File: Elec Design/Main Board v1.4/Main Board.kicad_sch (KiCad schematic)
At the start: 64 parts, among them J1 PJ-102A, J3 Conn_ARM_JTAG_SWD_10, J4 0022232041, SW1 SW_SPST, U1 BD9E302EFJ-E2, U2 ESP32-C3-MINI-1, U3 MCP2551-I-P, U4 NCP718xSN330, U5 LPC1768FBD100, Y1 12MHz/10pF, Y2 32.768kHz/9pF

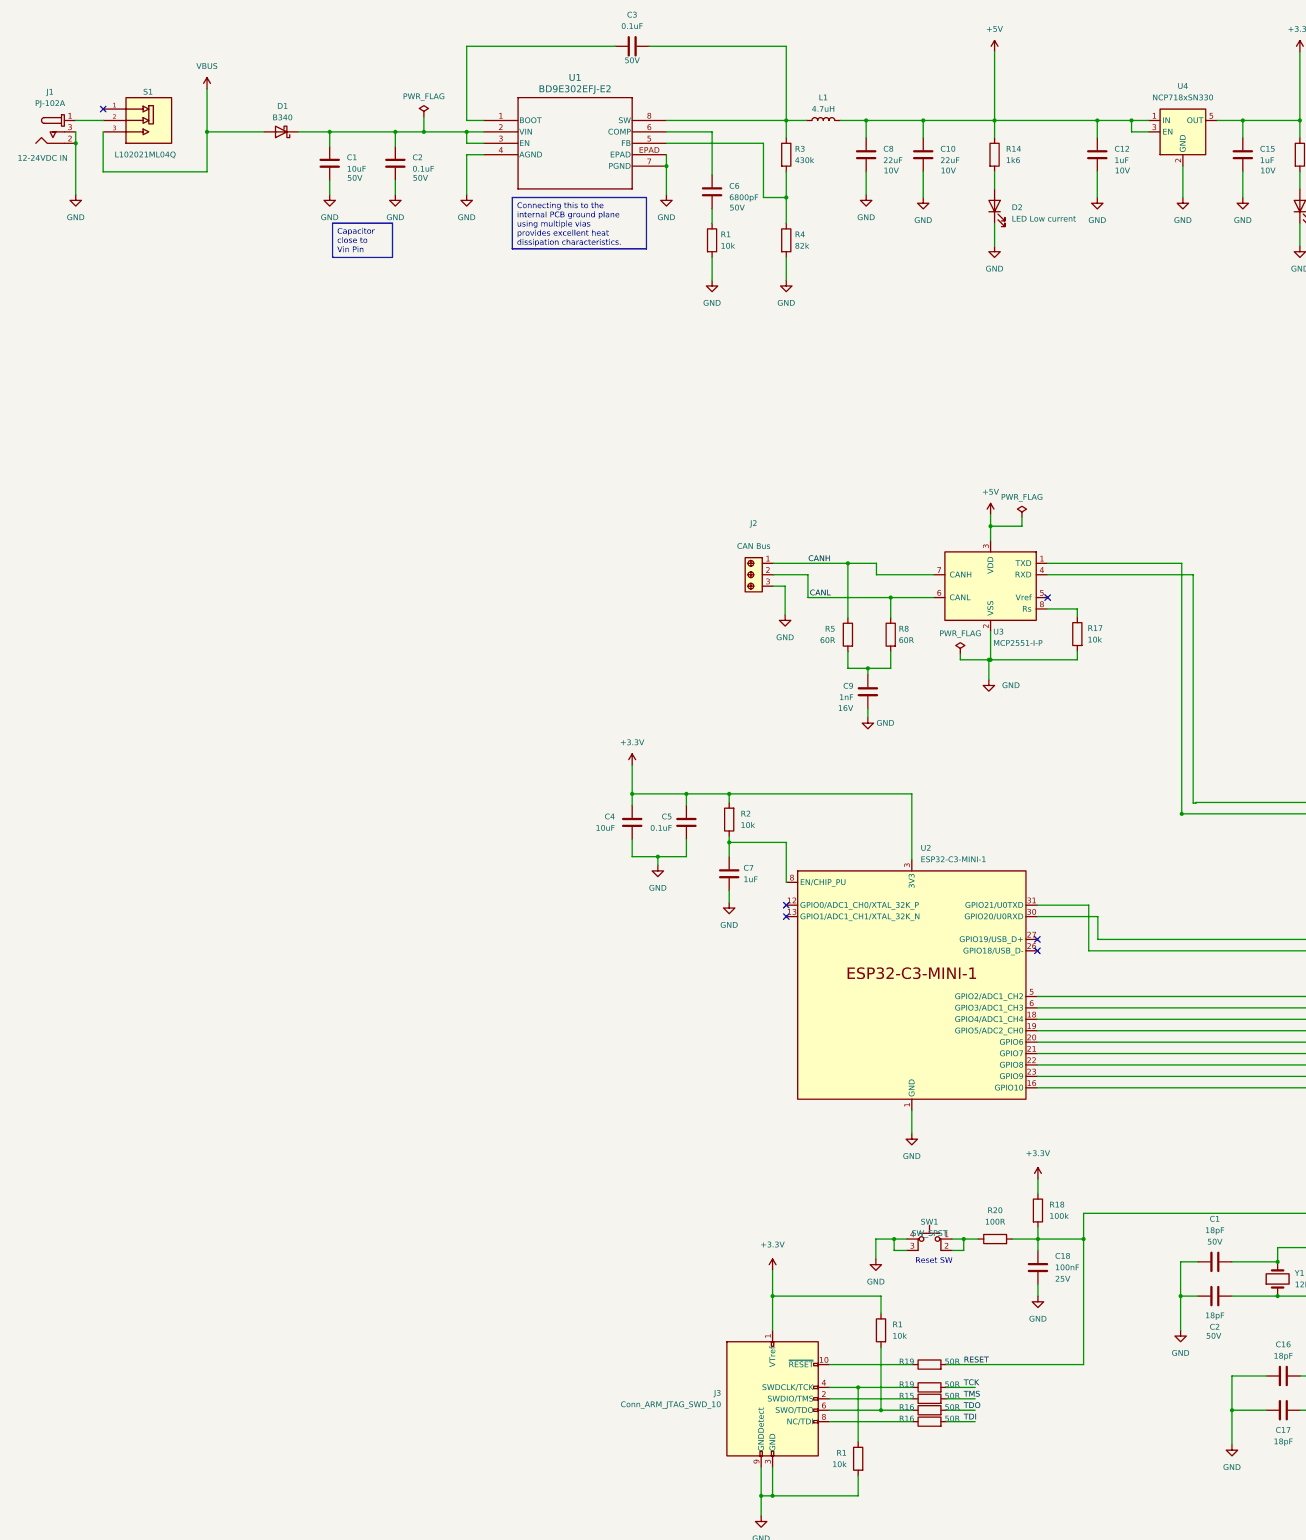
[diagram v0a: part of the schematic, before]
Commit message: fixed buck converter feedback position error
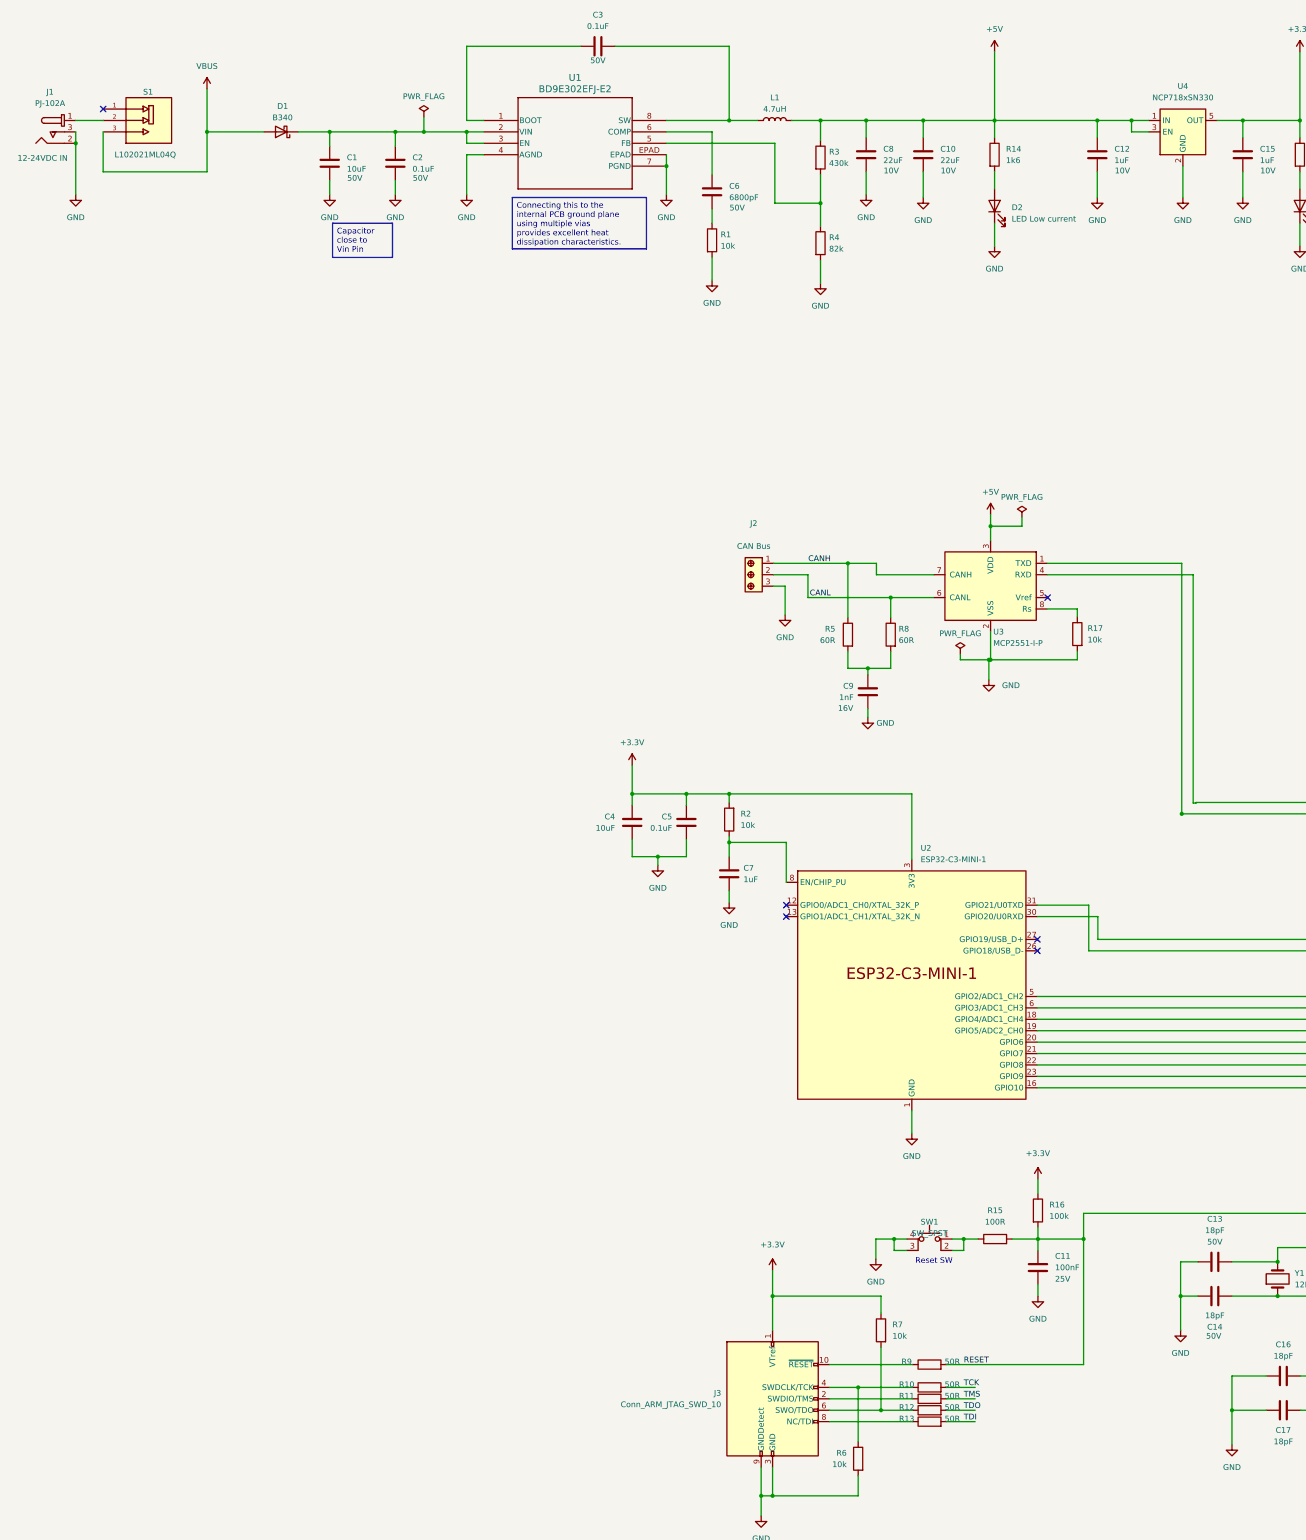
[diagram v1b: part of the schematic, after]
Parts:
- renumbered C18 to C11, C1 to C13, C2 to C14, R19 to R10, R15 to R11, R16 to R12, R16 to R13, R20 to R15, R18 to R16, R1 to R6, R1 to R7, R19 to R9
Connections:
- net +5V: now also R3.1
- net at C3.2, L1.1, U1.8 (SW): no longer R3.1
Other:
- moved on the sheet: C3, L1, R3, R4

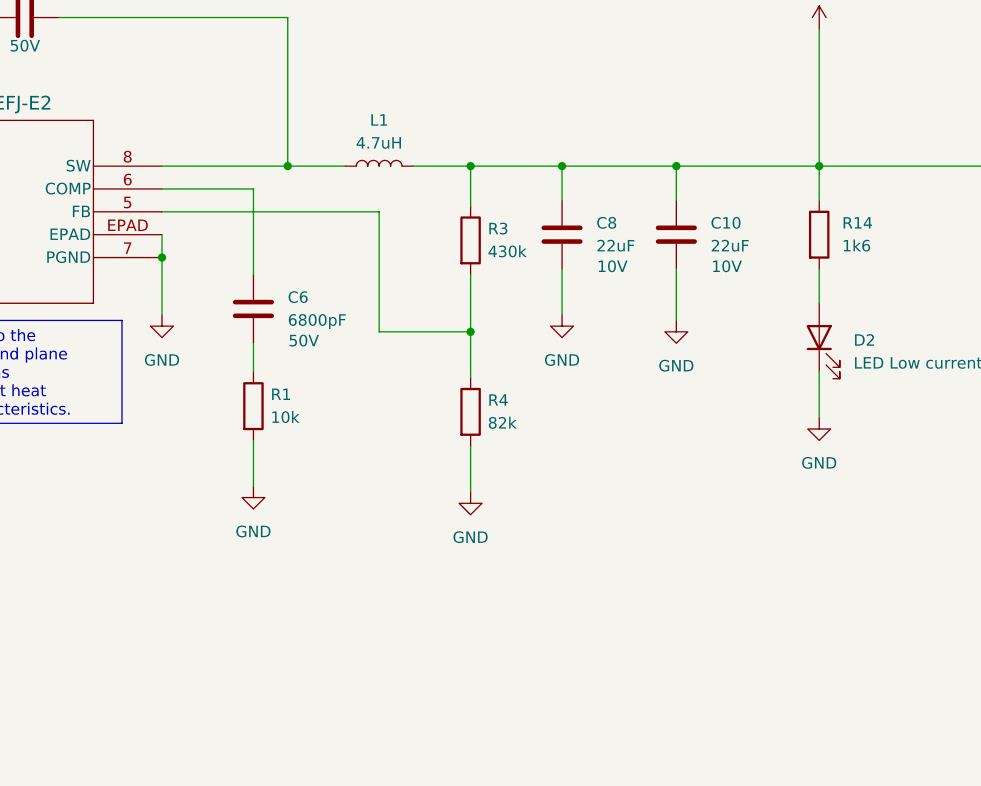
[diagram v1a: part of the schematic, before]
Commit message: updated schematic to fix buck fb point issue
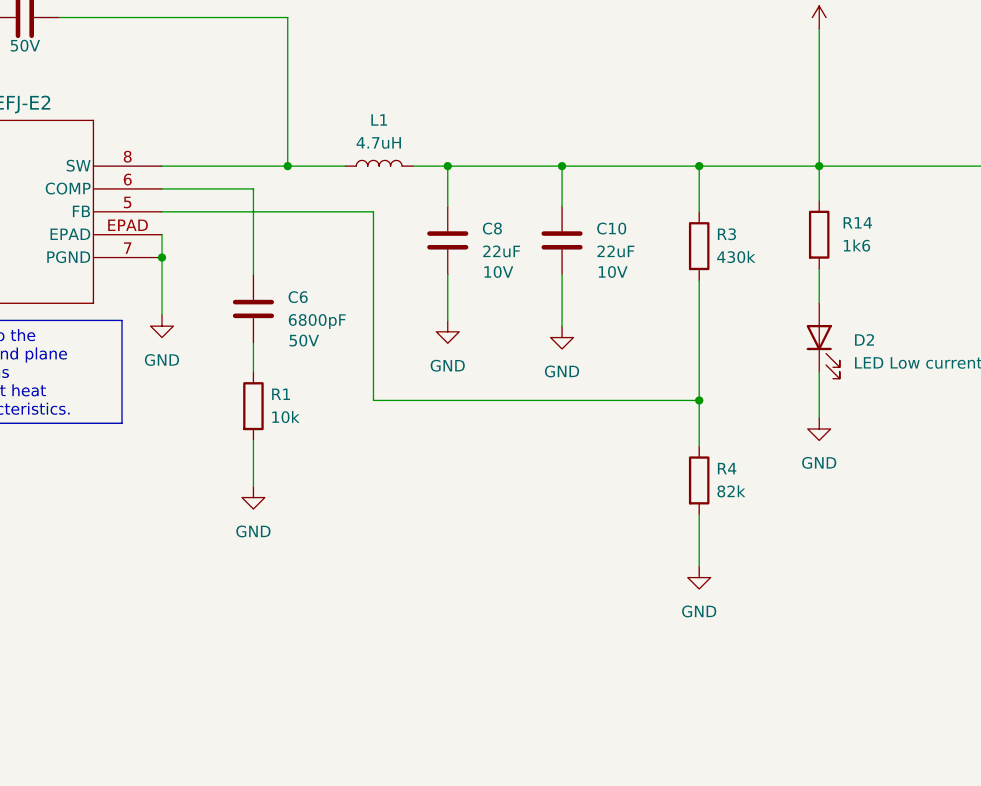
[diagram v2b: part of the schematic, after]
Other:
- moved on the sheet: C10, C8, R3, R4

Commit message: main board cleanup
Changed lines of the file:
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@@
 	)
 	(junction
-		(at 281.686 193.04)
-		(diameter 0)
-		(color 0 0 0 0)
-	)
-	(junction
 		(at 358.775 140.335)
 		(diameter 0)
@@
 	(wire
 		(pts
-			(xy 284.226 139.827) (xy 284.226 190.627)
+			(xy 284.226 139.827) (xy 284.226 190.5)
 		)
 		(stroke
@@
 	(wire
 		(pts
-			(xy 284.861 190.627) (xy 284.861 190.5)
-		)
-		(stroke
-			(width 0)
-			(type default)
-		)
-	)
-	(wire
-		(pts
 			(xy 394.97 162.56) (xy 407.035 162.56)
 		)
@@
 	(wire
 		(pts
-			(xy 281.686 193.167) (xy 281.686 193.04)
-		)
-		(stroke
-			(width 0)
-			(type default)
-		)
-	)
-	(wire
-		(pts
 			(xy 246.126 127.127) (xy 246.126 129.032)
 		)
@@
 	(wire
 		(pts
-			(xy 281.686 193.04) (xy 334.645 193.04)
-		)
-		(stroke
-			(width 0)
-			(type default)
-		)
-	)
-	(wire
-		(pts
 			(xy 240.03 50.165) (xy 240.03 53.975)
 		)
@@
 	(wire
 		(pts
-			(xy 281.686 137.287) (xy 251.841 137.287)
+			(xy 281.305 137.287) (xy 251.841 137.287)
 		)
 		(stroke
@@
 	(wire
 		(pts
-			(xy 284.861 190.5) (xy 334.645 190.5)
-		)
-		(stroke
-			(width 0)
-			(type default)
-		)
-	)
-	(wire
-		(pts
 			(xy 370.84 140.335) (xy 370.84 147.32)
 		)
@@
 	(wire
 		(pts
-			(xy 281.686 193.04) (xy 281.686 137.287)
+			(xy 281.305 137.287) (xy 281.305 193.04)
 		)
 		(stroke
@@
 	(wire
 		(pts
-			(xy 284.226 190.627) (xy 284.861 190.627)
+			(xy 284.226 190.5) (xy 334.645 190.5)
 		)
 		(stroke
@@
 		)
 		(stroke
+			(width 0)
+			(type default)
+		)
+	)
+	(wire
+		(pts
+			(xy 281.305 193.04) (xy 334.645 193.04)
+		)
+		(stroke
